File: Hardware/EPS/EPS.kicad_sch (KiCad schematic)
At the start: 2 parts

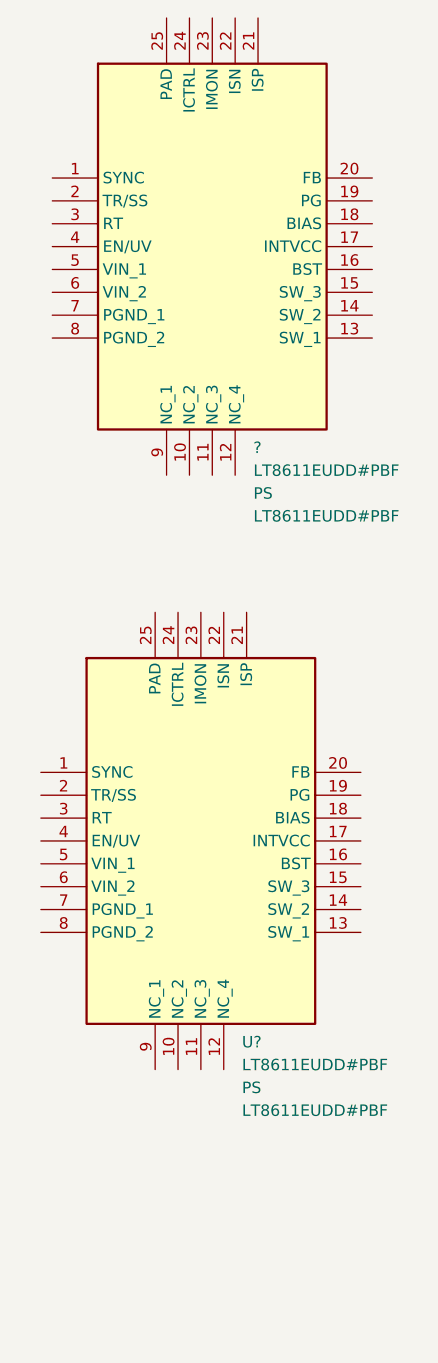
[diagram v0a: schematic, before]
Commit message: Edit README
Fixing README


Added LTC4162 footprint and symbol


README Edit


More README
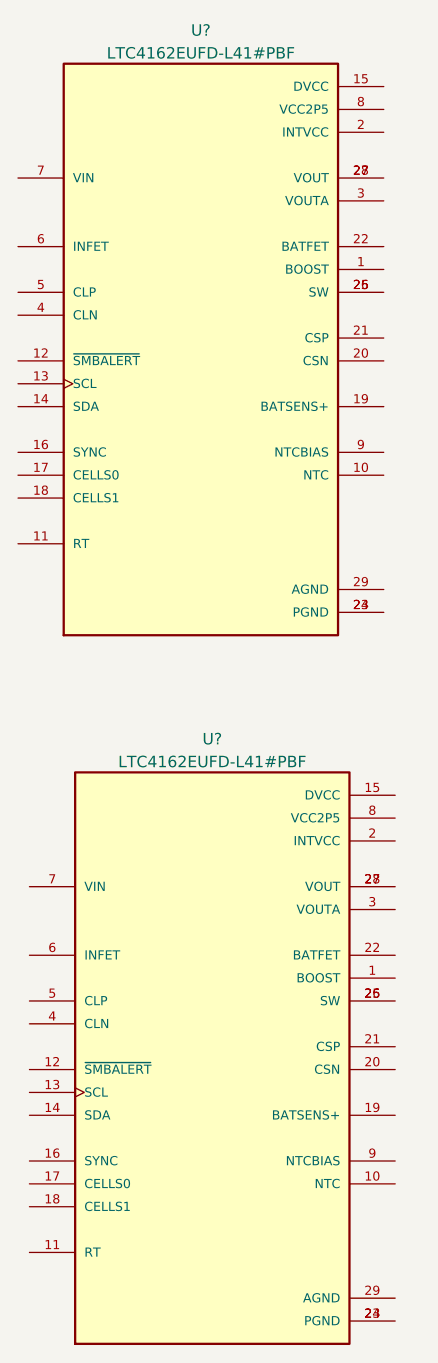
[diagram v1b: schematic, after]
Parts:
- removed ?, U?: LT8611EUDD#PBF, symbol LT8611EUDD#PBF:LT8611EUDD#PBF
- added U? (x2): LTC4162EUFD-L41#PBF, QFN50P500X400X80-29N, symbol LTC4162EUFD-L41_PBF:LTC4162EUFD-L41#PBF
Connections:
- new net: U?.23 (PGND), U?.24 (PGND) (x2)
- new net: U?.25 (SW), U?.26 (SW) (x2)
- new net: U?.27 (VOUT), U?.28 (VOUT) (x2)
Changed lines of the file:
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@@
 (kicad_sch (version 20211123) (generator eeschema)
   (paper "A4")
-  (symbol (lib_id "LT8611EUDD#PBF:LT8611EUDD#PBF") (at 67.31 46.99 0) (unit 1)
+  (symbol (lib_id "LTC4162EUFD-L41_PBF:LTC4162EUFD-L41#PBF") (at 85.09 143.51 0) (unit 1)
     (in_bom yes) (on_board yes) (fields_autoplaced)
-    (property "Reference" "?" (id 0) (at 89.6494 76.9604 0)
-      (effects (font (size 1.27 1.27)) (justify left))
+    (property "Reference" "U?" (id 0) (at 85.09 109.3302 0))
+    (property "Value" "LTC4162EUFD-L41#PBF" (id 1) (at 85.09 111.8671 0))
+    (property "Footprint" "QFN50P500X400X80-29N" (id 2) (at 85.09 143.51 0)
+      (effects (font (size 1.27 1.27)) (justify bottom) hide)
     )
-    (property "Value" "LT8611EUDD#PBF" (id 1) (at 89.6494 79.4973 0)
-      (effects (font (size 1.27 1.27)) (justify left))
-    )
-    (property "Footprint" "" (id 2) (at 67.31 46.99 0)
+    (property "Datasheet" "" (id 3) (at 85.09 143.51 0)
       (effects (font (size 1.27 1.27)) hide)
     )
-    (property "Datasheet" "" (id 3) (at 67.31 46.99 0)
-      (effects (font (size 1.27 1.27)) hide)
+    (property "MANUFACTURER" "Analog Devices" (id 4) (at 85.09 143.51 0)
+      (effects (font (size 1.27 1.27)) (justify bottom) hide)
     )
-    (property "Reference_1" "PS" (id 4) (at 89.6494 82.0342 0)
-      (effects (font (size 1.27 1.27)) (justify left))
+    (property "PARTREV" "A" (id 5) (at 85.09 143.51 0)
+      (effects (font (size 1.27 1.27)) (justify bottom) hide)
     )
-    (property "Value_1" "LT8611EUDD#PBF" (id 5) (at 89.6494 84.5711 0)
-      (effects (font (size 1.27 1.27)) (justify left))
-    )
-    (property "Footprint_1" "QFN50P300X500X80-25N-D" (id 6) (at 99.06 131.75 0)
-      (effects (font (size 1.27 1.27)) (justify left top) hide)
-    )
-    (property "Datasheet_1" "https://datasheet.datasheetarchive.com/originals/distributors/Datasheets-SFU1/DSASFU10008475.pdf" (id 7) (at 99.06 231.75 0)
-      (effects (font (size 1.27 1.27)) (justify left top) hide)
-    )
-    (property "Height" "0.8" (id 8) (at 99.06 431.75 0)
-      (effects (font (size 1.27 1.27)) (justify left top) hide)
-    )
-    (property "Manufacturer_Name" "Analog Devices" (id 9) (at 99.06 531.75 0)
-      (effects (font (size 1.27 1.27)) (justify left top) hide)
-    )
-    (property "Manufacturer_Part_Number" "LT8611EUDD#PBF" (id 10) (at 99.06 631.75 0)
-      (effects (font (size 1.27 1.27)) (justify left top) hide)
-    )
-    (property "Mouser Part Number" "584-LT8611EUDD#PBF" (id 11) (at 99.06 731.75 0)
-      (effects (font (size 1.27 1.27)) (justify left top) hide)
-    )
-    (property "Mouser Price/Stock" "https://www.mouser.co.uk/ProductDetail/Analog-Devices/LT8611EUDDPBF?qs=hVkxg5c3xu%252BxWd%2FGY0RL7A%3D%3D" (id 12) (at 99.06 831.75 0)
-      (effects (font (size 1.27 1.27)) (justify left top) hide)
-    )
-    (property "Arrow Part Number" "LT8611EUDD#PBF" (id 13) (at 99.06 931.75 0)
-      (effects (font (size 1.27 1.27)) (justify left top) hide)
-    )
-    (property "Arrow Price/Stock" "https://www.arrow.com/en/products/lt8611euddpbf/analog-devices?region=europe" (id 14) (at 99.06 1031.75 0)
-      (effects (font (size 1.27 1.27)) (justify left top) hide)
+    (property "STANDARD" "IPC-7351B" (id 6) (at 85.09 143.51 0)
+      (effects (font (size 1.27 1.27)) (justify bottom) hide)
     )
     (pin "1")
@@
     (pin "24")
     (pin "25")
+    (pin "26")
+    (pin "27")
+    (pin "28")
+    (pin "29")
     (pin "3")
     (pin "4")
@@
     (pin "9")
   )
-  (symbol (lib_id "LT8611EUDD#PBF:LT8611EUDD#PBF") (at 66.04 113.03 0) (unit 1)
+  (symbol (lib_id "LTC4162EUFD-L41_PBF:LTC4162EUFD-L41#PBF") (at 83.82 64.77 0) (unit 1)
     (in_bom yes) (on_board yes) (fields_autoplaced)
-    (property "Reference" "U?" (id 0) (at 88.3794 143.0004 0)
-      (effects (font (size 1.27 1.27)) (justify left))
+    (property "Reference" "U?" (id 0) (at 83.82 30.5902 0))
+    (property "Value" "LTC4162EUFD-L41#PBF" (id 1) (at 83.82 33.1271 0))
+    (property "Footprint" "QFN50P500X400X80-29N" (id 2) (at 83.82 64.77 0)
+      (effects (font (size 1.27 1.27)) (justify bottom) hide)
     )
-    (property "Value" "LT8611EUDD#PBF" (id 1) (at 88.3794 145.5373 0)
-      (effects (font (size 1.27 1.27)) (justify left))
-    )
-    (property "Footprint" "" (id 2) (at 66.04 113.03 0)
+    (property "Datasheet" "" (id 3) (at 83.82 64.77 0)
       (effects (font (size 1.27 1.27)) hide)
     )
-    (property "Datasheet" "" (id 3) (at 66.04 113.03 0)
-      (effects (font (size 1.27 1.27)) hide)
+    (property "MANUFACTURER" "Analog Devices" (id 4) (at 83.82 64.77 0)
+      (effects (font (size 1.27 1.27)) (justify bottom) hide)
     )
-    (property "Reference_1" "PS" (id 4) (at 88.3794 148.0742 0)
-      (effects (font (size 1.27 1.27)) (justify left))
+    (property "PARTREV" "A" (id 5) (at 83.82 64.77 0)
+      (effects (font (size 1.27 1.27)) (justify bottom) hide)
     )
-    (property "Value_1" "LT8611EUDD#PBF" (id 5) (at 88.3794 150.6111 0)
-      (effects (font (size 1.27 1.27)) (justify left))
-    )
-    (property "Footprint_1" "QFN50P300X500X80-25N-D" (id 6) (at 97.79 197.79 0)
-      (effects (font (size 1.27 1.27)) (justify left top) hide)
-    )
-    (property "Datasheet_1" "https://datasheet.datasheetarchive.com/originals/distributors/Datasheets-SFU1/DSASFU10008475.pdf" (id 7) (at 97.79 297.79 0)
-      (effects (font (size 1.27 1.27)) (justify left top) hide)
-    )
-    (property "Height" "0.8" (id 8) (at 97.79 497.79 0)
-      (effects (font (size 1.27 1.27)) (justify left top) hide)
-    )
-    (property "Manufacturer_Name" "Analog Devices" (id 9) (at 97.79 597.79 0)
-      (effects (font (size 1.27 1.27)) (justify left top) hide)
-    )
-    (property "Manufacturer_Part_Number" "LT8611EUDD#PBF" (id 10) (at 97.79 697.79 0)
-      (effects (font (size 1.27 1.27)) (justify left top) hide)
-    )
-    (property "Mouser Part Number" "584-LT8611EUDD#PBF" (id 11) (at 97.79 797.79 0)
-      (effects (font (size 1.27 1.27)) (justify left top) hide)
-    )
-    (property "Mouser Price/Stock" "https://www.mouser.co.uk/ProductDetail/Analog-Devices/LT8611EUDDPBF?qs=hVkxg5c3xu%252BxWd%2FGY0RL7A%3D%3D" (id 12) (at 97.79 897.79 0)
-      (effects (font (size 1.27 1.27)) (justify left top) hide)
-    )
-    (property "Arrow Part Number" "LT8611EUDD#PBF" (id 13) (at 97.79 997.79 0)
-      (effects (font (size 1.27 1.27)) (justify left top) hide)
-    )
-    (property "Arrow Price/Stock" "https://www.arrow.com/en/products/lt8611euddpbf/analog-devices?region=europe" (id 14) (at 97.79 1097.79 0)
-      (effects (font (size 1.27 1.27)) (justify left top) hide)
+    (property "STANDARD" "IPC-7351B" (id 6) (at 83.82 64.77 0)
+      (effects (font (size 1.27 1.27)) (justify bottom) hide)
     )
     (pin "1")
@@
     (pin "24")
     (pin "25")
+    (pin "26")
+    (pin "27")
+    (pin "28")
+    (pin "29")
     (pin "3")
     (pin "4")
@@
   )
   (symbol_instances
-    (path "/2cc3cfdf-06da-4e4b-8014-93ea8811695c"
-      (reference "?") (unit 1) (value "LT8611EUDD#PBF") (footprint "")
+    (path "/1df6c9c1-e135-42aa-9128-090e1ffdba0c"
+      (reference "U?") (unit 1) (value "LTC4162EUFD-L41#PBF") (footprint "QFN50P500X400X80-29N")
     )
-    (path "/5ab2c61c-de11-4475-aca0-db702cf5c553"
-      (reference "U?") (unit 1) (value "LT8611EUDD#PBF") (footprint "")
+    (path "/5c57082f-2c5a-4527-87aa-8948b2152f21"
+      (reference "U?") (unit 1) (value "LTC4162EUFD-L41#PBF") (footprint "QFN50P500X400X80-29N")
     )
   )

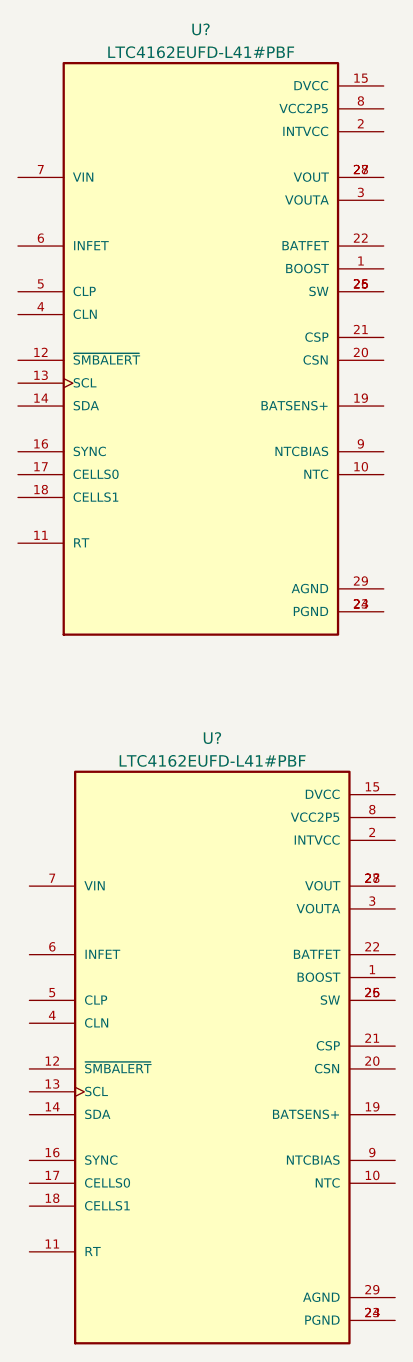
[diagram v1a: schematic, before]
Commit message: Created Schematic for LTC4162
Added Comments
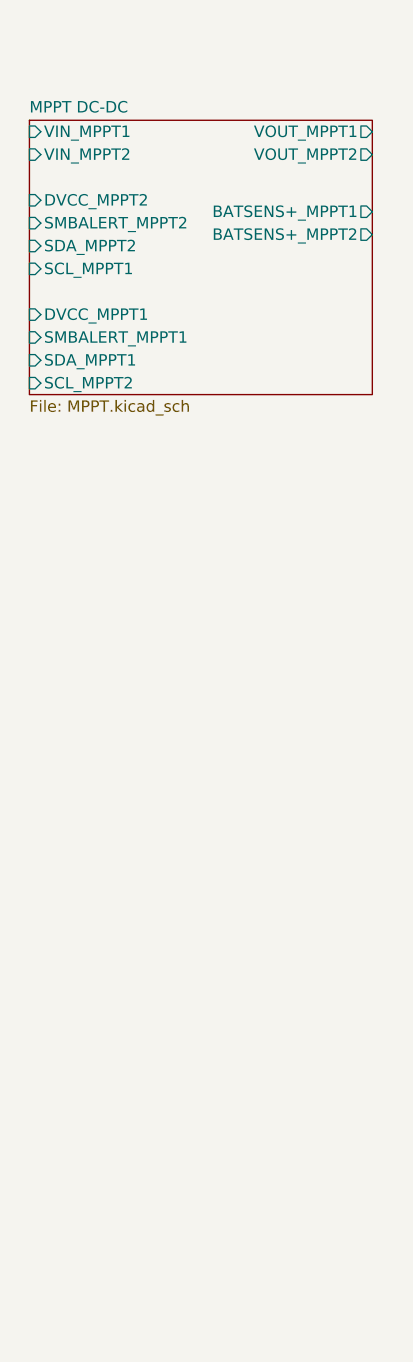
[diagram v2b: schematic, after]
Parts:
- removed U? (x2): LTC4162EUFD-L41#PBF, QFN50P500X400X80-29N, symbol LTC4162EUFD-L41_PBF:LTC4162EUFD-L41#PBF
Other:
- added sheet MPPT DC-DC (MPPT.kicad_sch)

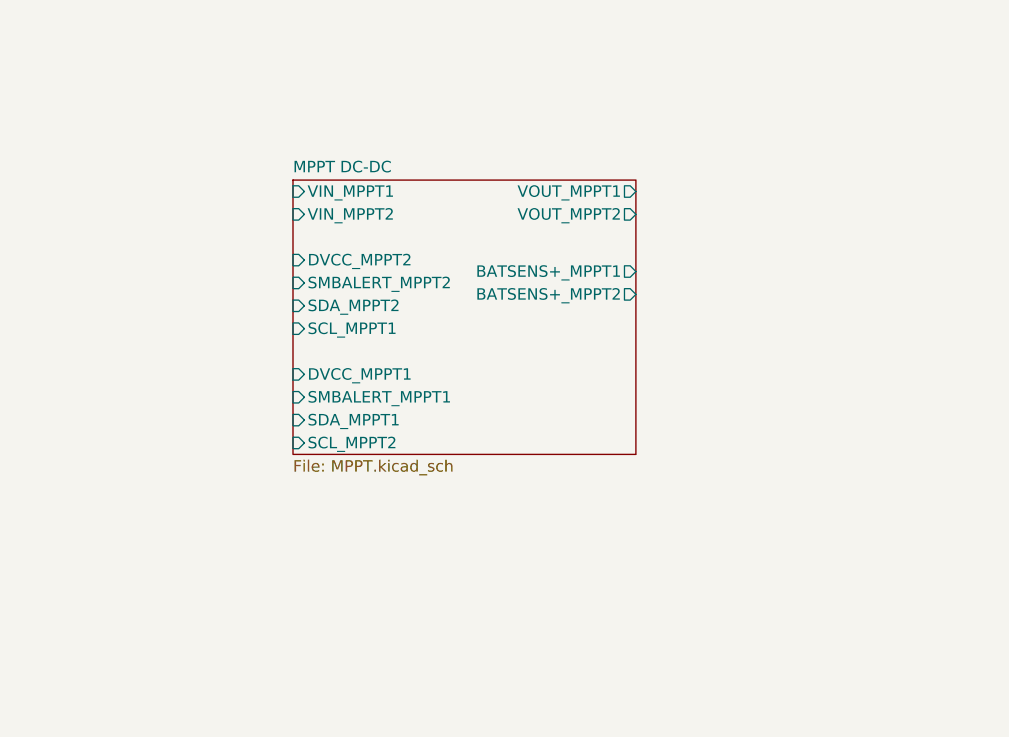
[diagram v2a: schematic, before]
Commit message: Added USB, Solar Connector and MATLAB Folder
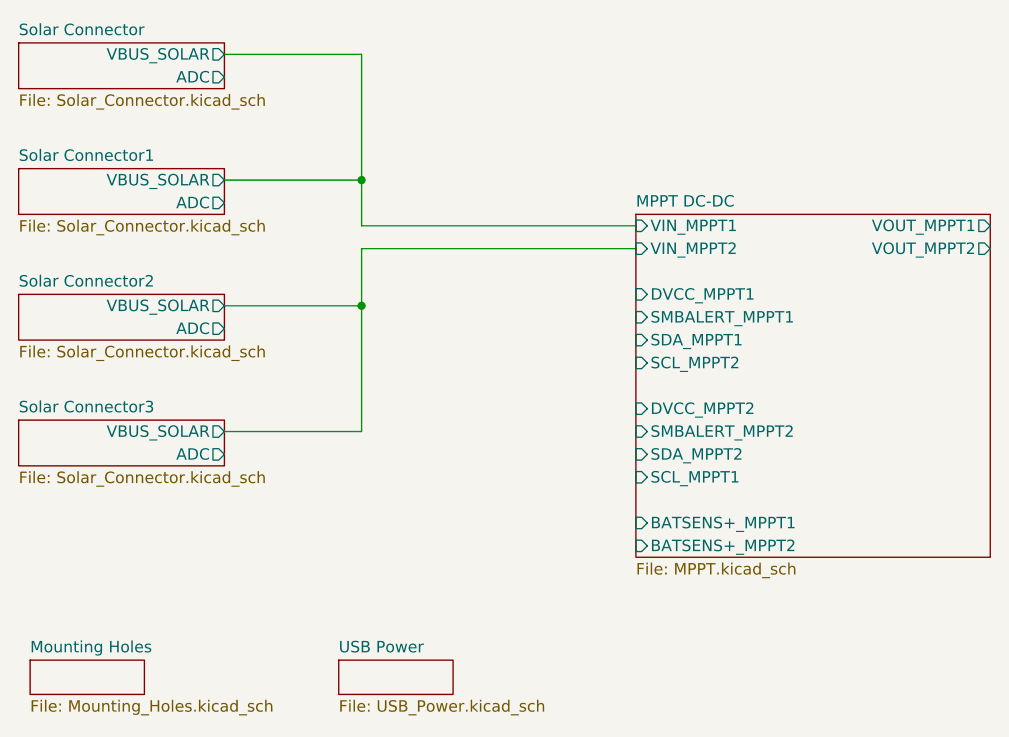
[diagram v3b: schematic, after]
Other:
- added sheet Mounting Holes (Mounting_Holes.kicad_sch)
- added sheet Solar Connector (Solar_Connector.kicad_sch)
- added sheet Solar Connector1 (Solar_Connector.kicad_sch)
- added sheet Solar Connector2 (Solar_Connector.kicad_sch)
- added sheet Solar Connector3 (Solar_Connector.kicad_sch)
- added sheet USB Power (USB_Power.kicad_sch)

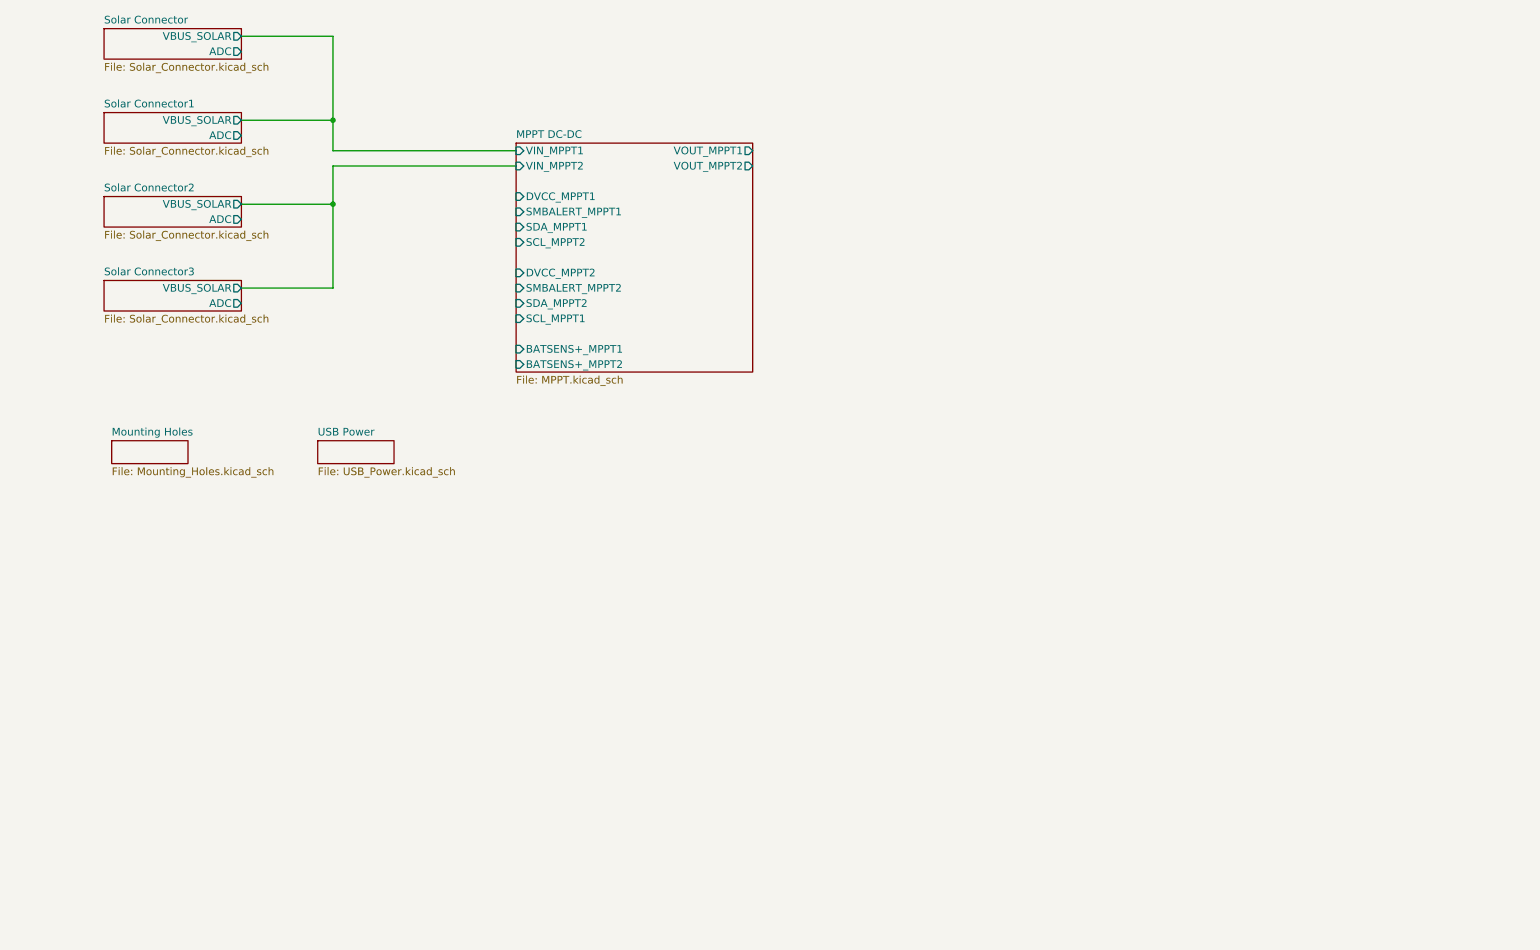
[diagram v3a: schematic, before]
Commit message: Added interboard connector and MCU
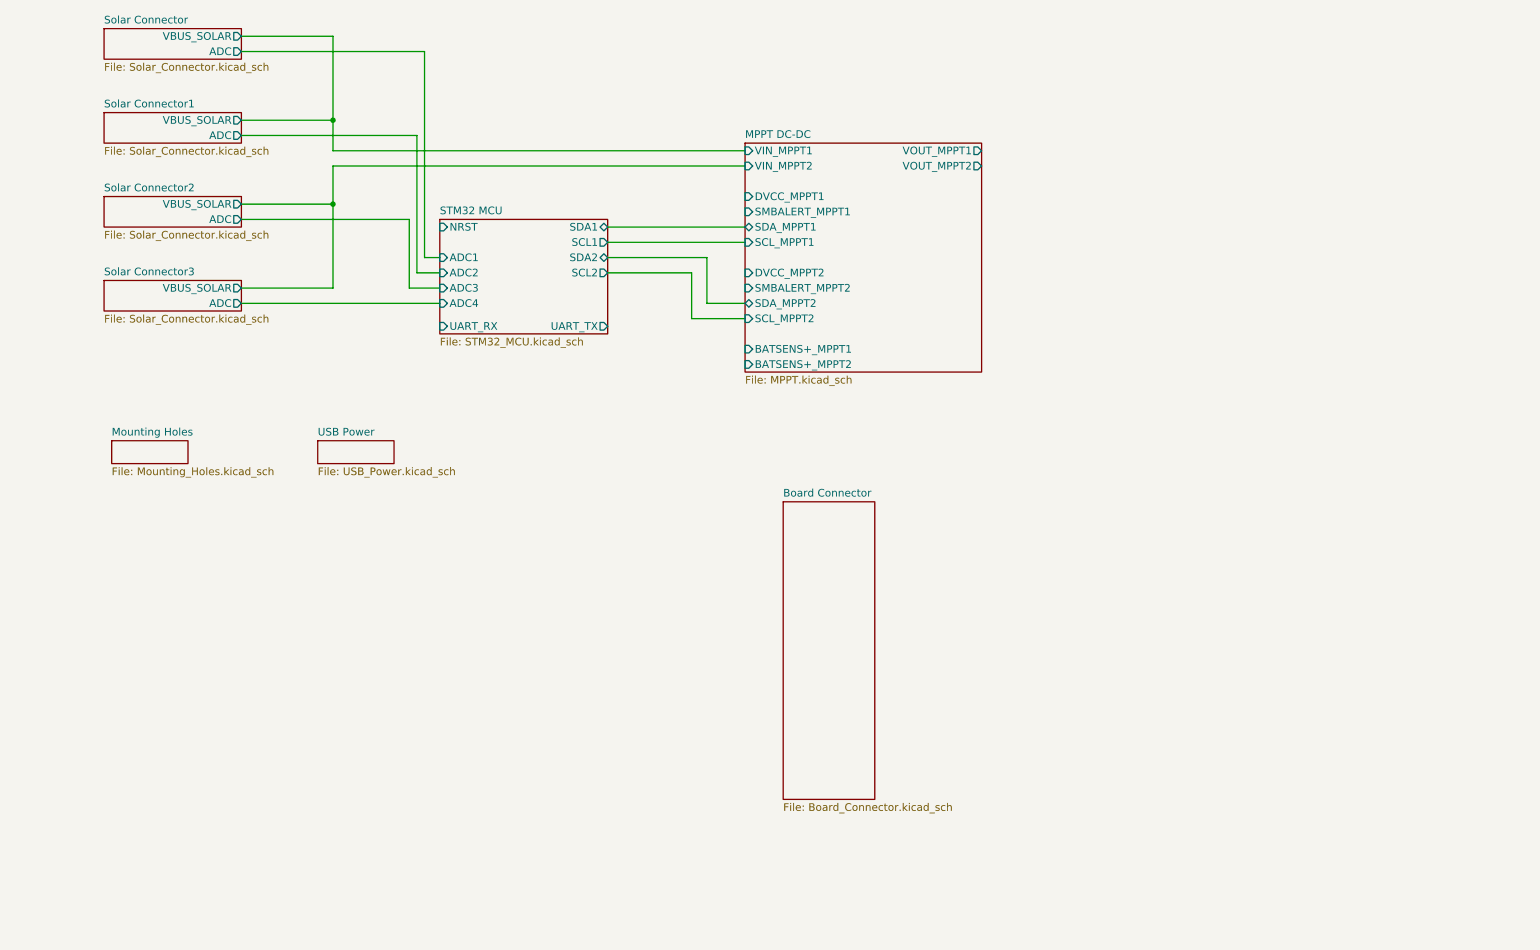
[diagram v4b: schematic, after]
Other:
- added sheet Board Connector (Board_Connector.kicad_sch)
- added sheet STM32 MCU (STM32_MCU.kicad_sch)
